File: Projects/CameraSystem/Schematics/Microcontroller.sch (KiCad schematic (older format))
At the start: 24 parts, among them J2 Conn_02x03_Odd_Even, J3 Conn_01x02, J4 Conn_01x03, J5 Conn_01x02, SW1 SW_Push, U3 ATMEGA16A-AU, Y2 ABLS2-10.000MHZ-D4Y-T

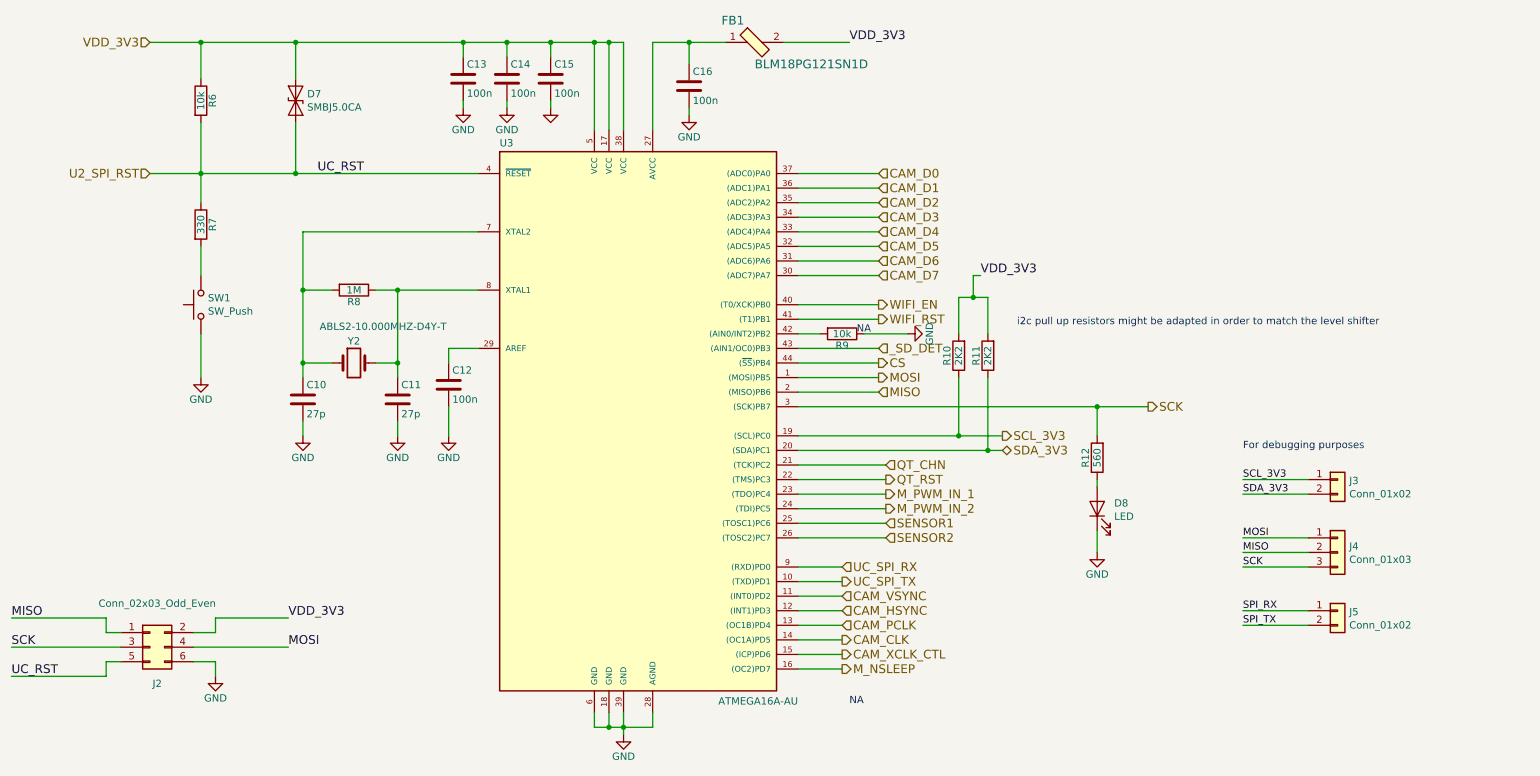
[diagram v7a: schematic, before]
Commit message: camera was updated
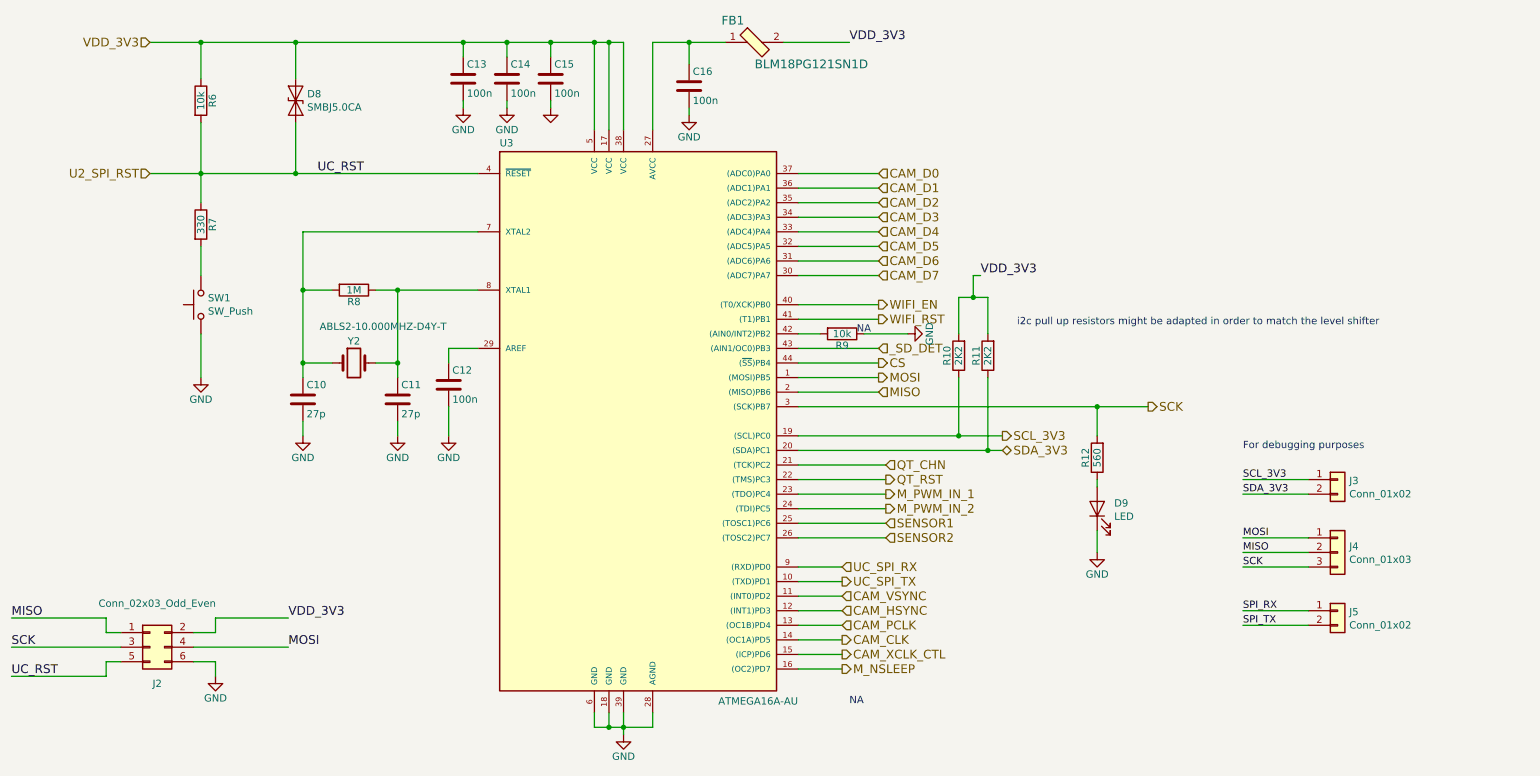
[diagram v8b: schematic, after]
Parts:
- J4: footprint Connector_PinSocket_2.54mm:PinSocket_1x03_P2.54mm_Horizontal -> Connector_PinSocket_2.54mm:PinSocket_1x03_P2.54mm_Vertical
- renumbered D7 to D8, D8 to D9
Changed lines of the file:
@@
 F 0 "J4" H 10130 4342 50  0000 L CNN
 F 1 "Conn_01x03" H 10130 4251 50  0000 L CNN
-F 2 "Connector_PinSocket_2.54mm:PinSocket_1x03_P2.54mm_Horizontal" H 10050 4300 50  0001 C CNN
+F 2 "Connector_PinSocket_2.54mm:PinSocket_1x03_P2.54mm_Vertical" H 10050 4300 50  0001 C CNN
 F 3 "~" H 10050 4300 50  0001 C CNN
 	1    10050 4300
@@
 	2250 800  2900 800
 $Comp
-L Device:LED D8
+L Device:LED D9
 U 1 1 5CA538DC
 P 8400 4000
-F 0 "D8" V 8438 3883 50  0000 R CNN
+F 0 "D9" V 8438 3883 50  0000 R CNN
 F 1 "LED" V 8347 3883 50  0000 R CNN
 F 2 "LED_SMD:LED_1206_3216Metric" H 8400 4000 50  0001 C CNN
@@
 $EndComp
 $Comp
-L Device:D_TVS D7
+L Device:D_TVS D8
 U 1 1 5CA48BC2
 P 2900 1200
-F 0 "D7" V 2854 1279 50  0000 L CNN
+F 0 "D8" V 2854 1279 50  0000 L CNN
 F 1 "SMBJ5.0CA" V 2945 1279 50  0000 L CNN
 F 2 "custom-footprints:SMB_DO-214AA" H 2900 1200 50  0001 C CNN
